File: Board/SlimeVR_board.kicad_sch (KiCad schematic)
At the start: 36 parts, among them IC1 HT7833, J1 USB_C_Receptacle_USB2.0_16P, J2 JST-PH, J3 SMD_Pads, J4 SMD_Pads, J5 Conn_01x01_Pin, J6 Conn_01x01_Pin, J7 JTX-HX-A-1, J8 JTX-HX-A-1, Q1 DMP3099L-7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

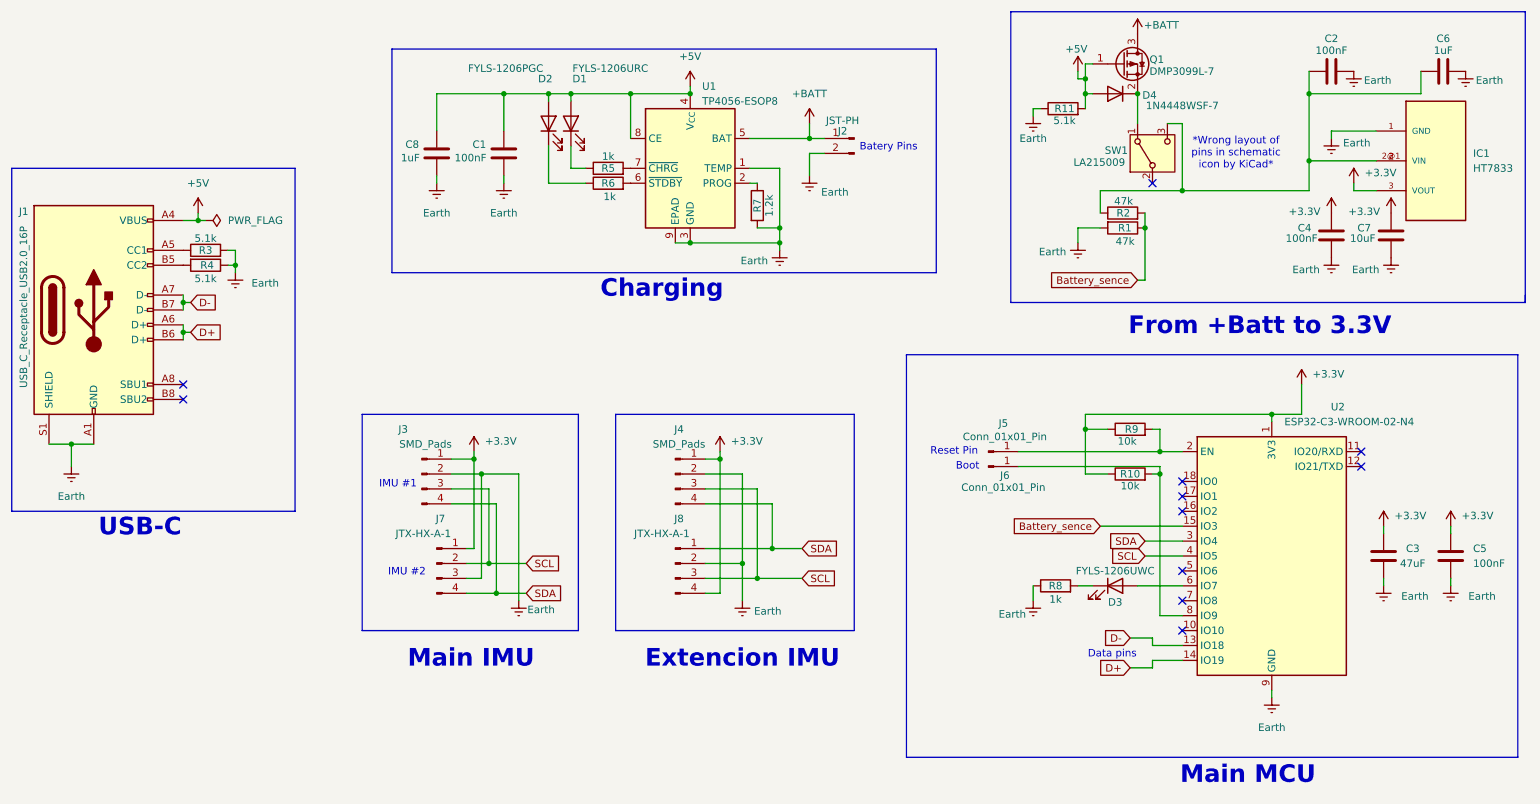
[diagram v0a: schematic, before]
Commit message: Redisign, Power Supply improved
Removed reset pin becuse just hardware off > on
Added physical button for boot
HT7833 replaced for XC6220B331MR becuse HT7833 not working :(
Small design silkscreen changes
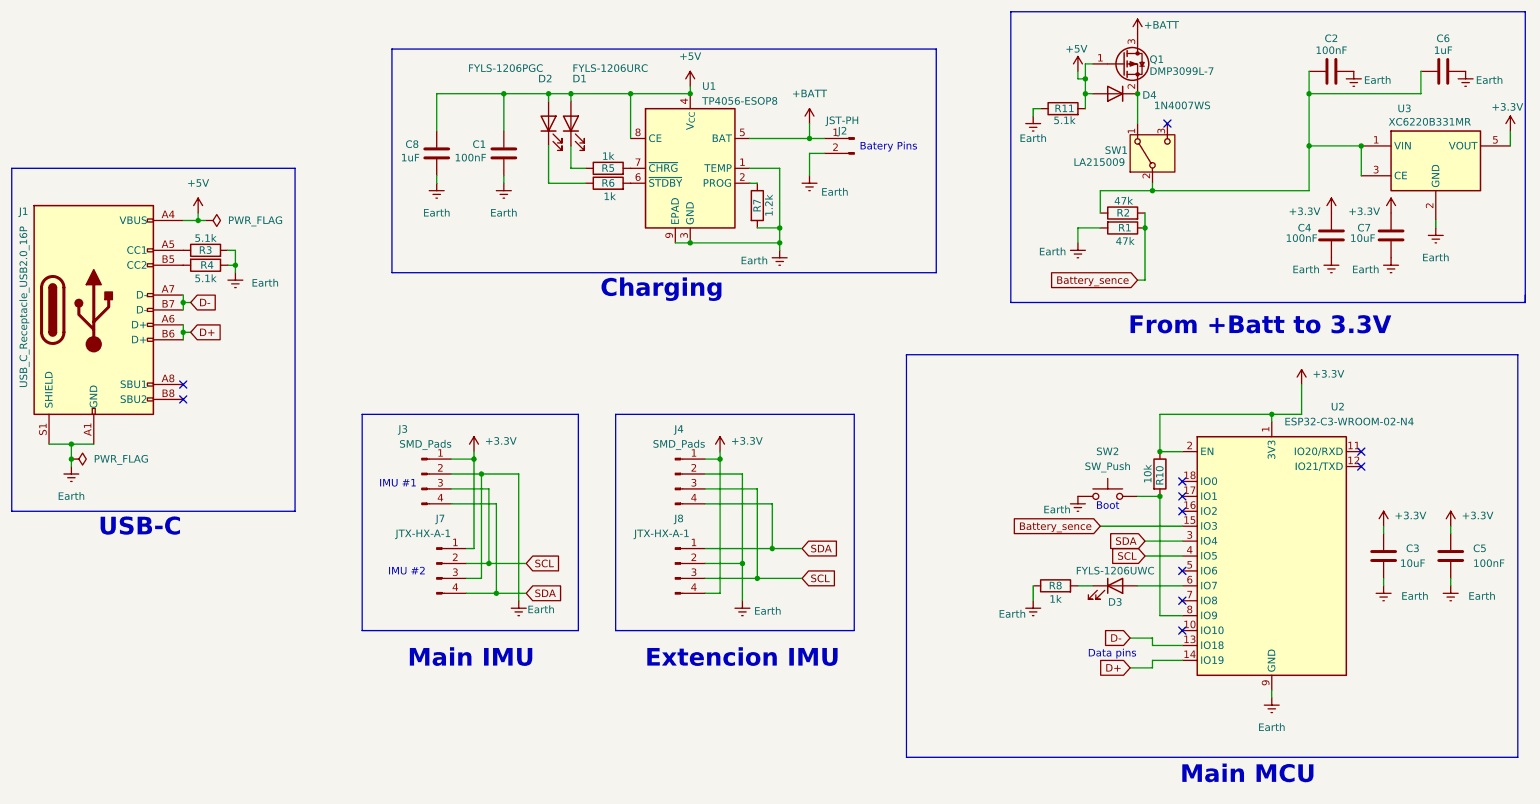
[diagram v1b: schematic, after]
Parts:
- removed IC1: HT7833, Package_TO_SOT_SMD:SOT-89-3_Handsoldering, symbol HT7833:HT7833
- removed J5, J6: Conn_01x01_Pin, TestPoint:TestPoint_Pad_1.5x1.5mm, symbol Connector:Conn_01x01_Pin
- removed R9: 10k, Resistor_SMD:R_0805_2012Metric_Pad1.20x1.40mm_HandSolder, symbol Device:R
- added SW2: SW_Push, Button_Switch_SMD:SW_Push_1P1T_XKB_TS-1187A, symbol Switch:SW_Push
- added U3: XC6220B331MR, Package_TO_SOT_SMD:SOT-23-5, symbol Regulator_Linear:XC6220B331MR
- C3: value 47uF -> 10uF
- D4: value 1N4448WSF-7 -> 1N4007WS; Source https://www.tme.eu/cz/details/1n4148wsq-7-f/univerzalni-dio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 -> https://www.tme.eu/cz/details/1n4007ws
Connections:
- net +3.3V: now also U2.2 (EN), U3.5 (VOUT)
- net Earth: now also SW2.1, U3.2 (GND)
- net at C2.1, C6.1, R2.1: now also SW1.2 (B), U3.1 (VIN), U3.3 (CE); no longer SW1.3 (C)
- net at R10.2, U2.8 (IO9): now also SW2.2
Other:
- note removed: "*Wrong layout of pins in schematic icon by KiCad*"
- note removed: "Reset Pin"
- moved on the sheet: R10
